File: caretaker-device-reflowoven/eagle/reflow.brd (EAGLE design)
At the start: 80 x 50 mm, 30 parts, among them IC1 ATmega328P-20PU, IC3 MCP1702-3302, Q1 16MHz, T1 TIP110

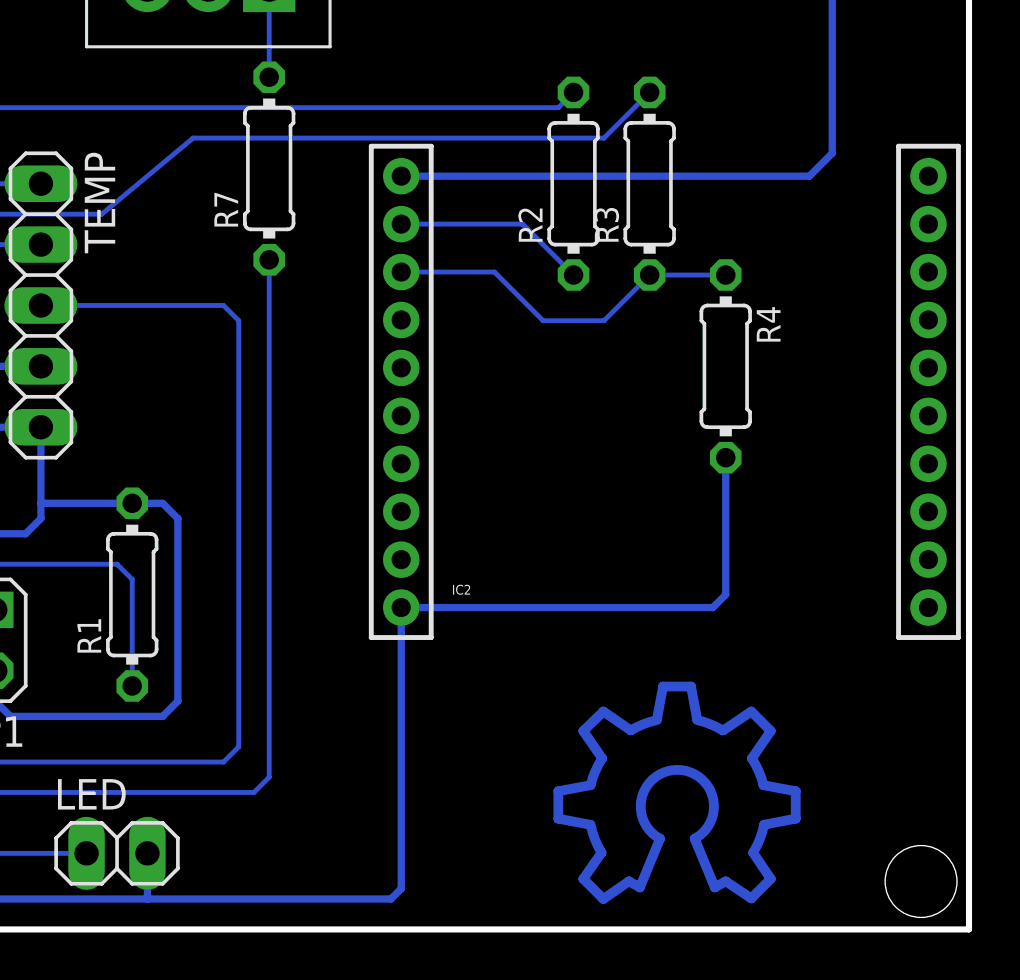
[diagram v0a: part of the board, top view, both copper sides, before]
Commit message: feat: Convert the XBee Reflow Oven device to a WLAN device fix: LCD flickering
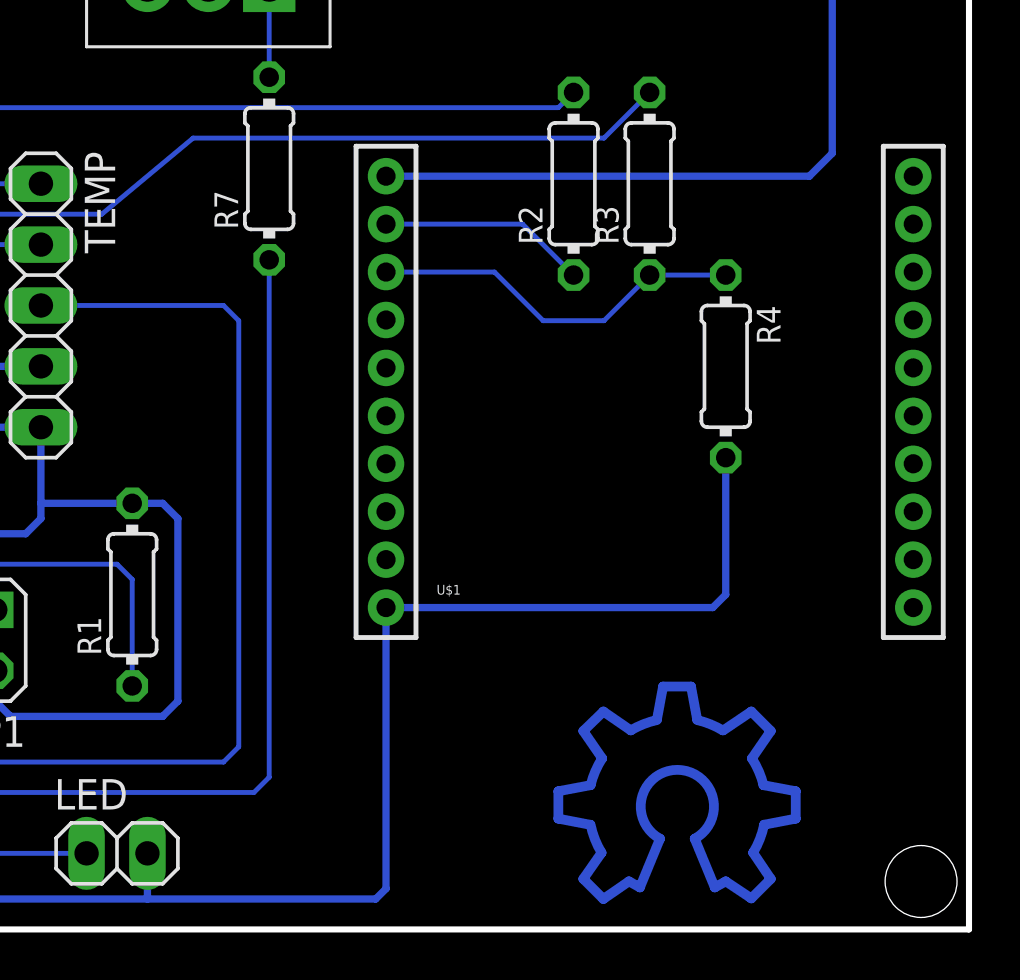
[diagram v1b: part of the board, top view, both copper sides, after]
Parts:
- removed IC2: (no value), SparkFun:XBEE-1
- added U$1: WIFLY-TH, grapelabs:WIFLY-TH
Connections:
- net +3V3: now also U$1.1; no longer IC2.1
- net GND: now also U$1.10; no longer IC2.10
- net N$4: now also U$1.3; no longer IC2.3
- net N$5: now also U$1.2; no longer IC2.2
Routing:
- net N$5: track 8.07 -> 8.71 mm
- net N$4: track 15.2 -> 15.8 mm
- net +3V3: track 39.0 -> 39.6 mm
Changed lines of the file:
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@@
 <?xml version="1.0" encoding="utf-8"?>
 <!DOCTYPE eagle SYSTEM "eagle.dtd">
-<eagle version="6.4">
+<eagle version="6.5.0">
 <drawing>
 <settings>
@@
 <element name="BACKLIGHT" library="pinhead" package="1X02" value="" x="5.715" y="35.941" rot="R270"/>
 <element name="KEYS" library="pinhead" package="1X05" value="" x="31.75" y="45.72"/>
-<element name="IC2" library="SparkFun" package="XBEE-1" value="" x="67.31" y="11.43"/>
 <element name="IC1" library="atmega8" package="DIL28-3" value="ATmega328P-20PU" x="24.765" y="19.685" rot="R270"/>
 <element name="Q1" library="crystal" package="HC49U-V" value="16MHz" x="15.24" y="14.605" rot="R90"/>
@@
 <element name="PWR12V" library="pinhead" package="1X02" value="" x="44.45" y="45.72"/>
 <element name="LOGO1" library="OSHW" package="OSHW_10X350_NOTEXT_BOTTOM" value="OSHW_LOGO_10MILX0350-NT-BOTTOM" x="67.945" y="5.08"/>
+<element name="U$1" library="grapelabs" package="WIFLY-TH" value="WIFLY-TH" x="66.675" y="11.43"/>
 </elements>
 <signals>
@@
 <contactref element="C2" pad="1"/>
 <contactref element="ICSP1" pad="6"/>
-<contactref element="IC2" pad="10"/>
 <contactref element="R4" pad="2"/>
 <contactref element="C5" pad="-"/>
@@
 <wire x1="60.96" y1="43.815" x2="67.31" y2="43.815" width="0.3048" layer="16"/>
 <wire x1="67.31" y1="43.815" x2="72.39" y2="43.815" width="0.3048" layer="16"/>
-<wire x1="56.31" y1="13.43" x2="69.31" y2="13.43" width="0.3048" layer="16"/>
 <wire x1="69.31" y1="13.43" x2="69.85" y2="13.97" width="0.3048" layer="16"/>
 <wire x1="69.85" y1="13.97" x2="69.85" y2="19.685" width="0.3048" layer="16"/>
@@
 <wire x1="25.4" y1="1.27" x2="45.72" y2="1.27" width="0.3048" layer="16"/>
 <wire x1="45.72" y1="3.175" x2="45.72" y2="1.27" width="0.3048" layer="16"/>
-<wire x1="56.31" y1="13.43" x2="56.31" y2="1.7" width="0.3048" layer="16"/>
-<wire x1="56.31" y1="1.7" x2="55.88" y2="1.27" width="0.3048" layer="16"/>
-<wire x1="55.88" y1="1.27" x2="45.72" y2="1.27" width="0.3048" layer="16"/>
 <wire x1="22.86" y1="14.605" x2="22.86" y2="10.16" width="0.3048" layer="16"/>
 <wire x1="22.86" y1="10.16" x2="23.495" y2="9.525" width="0.3048" layer="16"/>
@@
 <wire x1="24.765" y1="1.27" x2="25.4" y2="1.27" width="0.3048" layer="16"/>
 <wire x1="45.72" y1="45.72" x2="45.72" y2="47.9425" width="0.3048" layer="16"/>
+<contactref element="U$1" pad="10"/>
+<contactref element="U$1" pad="10"/>
+<wire x1="45.72" y1="1.27" x2="55.245" y2="1.27" width="0.3048" layer="16"/>
+<wire x1="55.675" y1="13.43" x2="55.675" y2="1.7" width="0.3048" layer="16"/>
+<wire x1="55.675" y1="1.7" x2="55.245" y2="1.27" width="0.3048" layer="16"/>
+<wire x1="69.31" y1="13.43" x2="55.675" y2="13.43" width="0.3048" layer="16"/>
 </signal>
 <signal name="MISO">
@@
 </signal>
 <signal name="N$4">
-<contactref element="IC2" pad="3"/>
 <contactref element="R3" pad="1"/>
 <contactref element="R4" pad="1"/>
-<wire x1="56.31" y1="27.43" x2="60.2" y2="27.43" width="0.2032" layer="16"/>
 <wire x1="60.2" y1="27.43" x2="62.23" y2="25.4" width="0.2032" layer="16"/>
 <wire x1="62.23" y1="25.4" x2="64.77" y2="25.4" width="0.2032" layer="16"/>
 <wire x1="64.77" y1="25.4" x2="66.675" y2="27.305" width="0.2032" layer="16"/>
 <wire x1="66.675" y1="27.305" x2="69.85" y2="27.305" width="0.2032" layer="16"/>
+<contactref element="U$1" pad="3"/>
+<wire x1="60.2" y1="27.43" x2="55.675" y2="27.43" width="0.2032" layer="16"/>
 </signal>
 <signal name="N$5">
 <contactref element="R2" pad="1"/>
-<contactref element="IC2" pad="2"/>
-<wire x1="56.31" y1="29.43" x2="61.375" y2="29.43" width="0.2032" layer="16"/>
 <wire x1="61.375" y1="29.43" x2="63.5" y2="27.305" width="0.2032" layer="16"/>
+<contactref element="U$1" pad="2"/>
+<wire x1="61.375" y1="29.43" x2="55.675" y2="29.43" width="0.2032" layer="16"/>
 </signal>
 <signal name="+3V3">
-<contactref element="IC2" pad="1"/>
 <contactref element="IC3" pad="VOUT"/>
 <contactref element="C5" pad="+"/>
@@
 <wire x1="73.66" y1="46.355" x2="72.39" y2="46.355" width="0.3048" layer="16"/>
 <wire x1="74.295" y1="45.72" x2="73.66" y2="46.355" width="0.3048" layer="16"/>
-<wire x1="56.31" y1="31.43" x2="73.34" y2="31.43" width="0.3048" layer="16"/>
 <wire x1="73.34" y1="31.43" x2="74.295" y2="32.385" width="0.3048" layer="16"/>
 <wire x1="74.295" y1="32.385" x2="74.295" y2="45.72" width="0.3048" layer="16"/>
+<contactref element="U$1" pad="1"/>
+<wire x1="73.34" y1="31.43" x2="55.675" y2="31.43" width="0.3048" layer="16"/>
 </signal>
 <signal name="BUTTON4">
